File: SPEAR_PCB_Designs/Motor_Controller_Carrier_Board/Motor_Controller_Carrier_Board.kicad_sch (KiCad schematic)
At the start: 15 parts, among them J1 Conn_01x02_Pin, J2 Conn_01x02_Pin, J3 Conn_01x02_Pin, J4 JST_S4B-XH-A-1, U1 AP63203WU

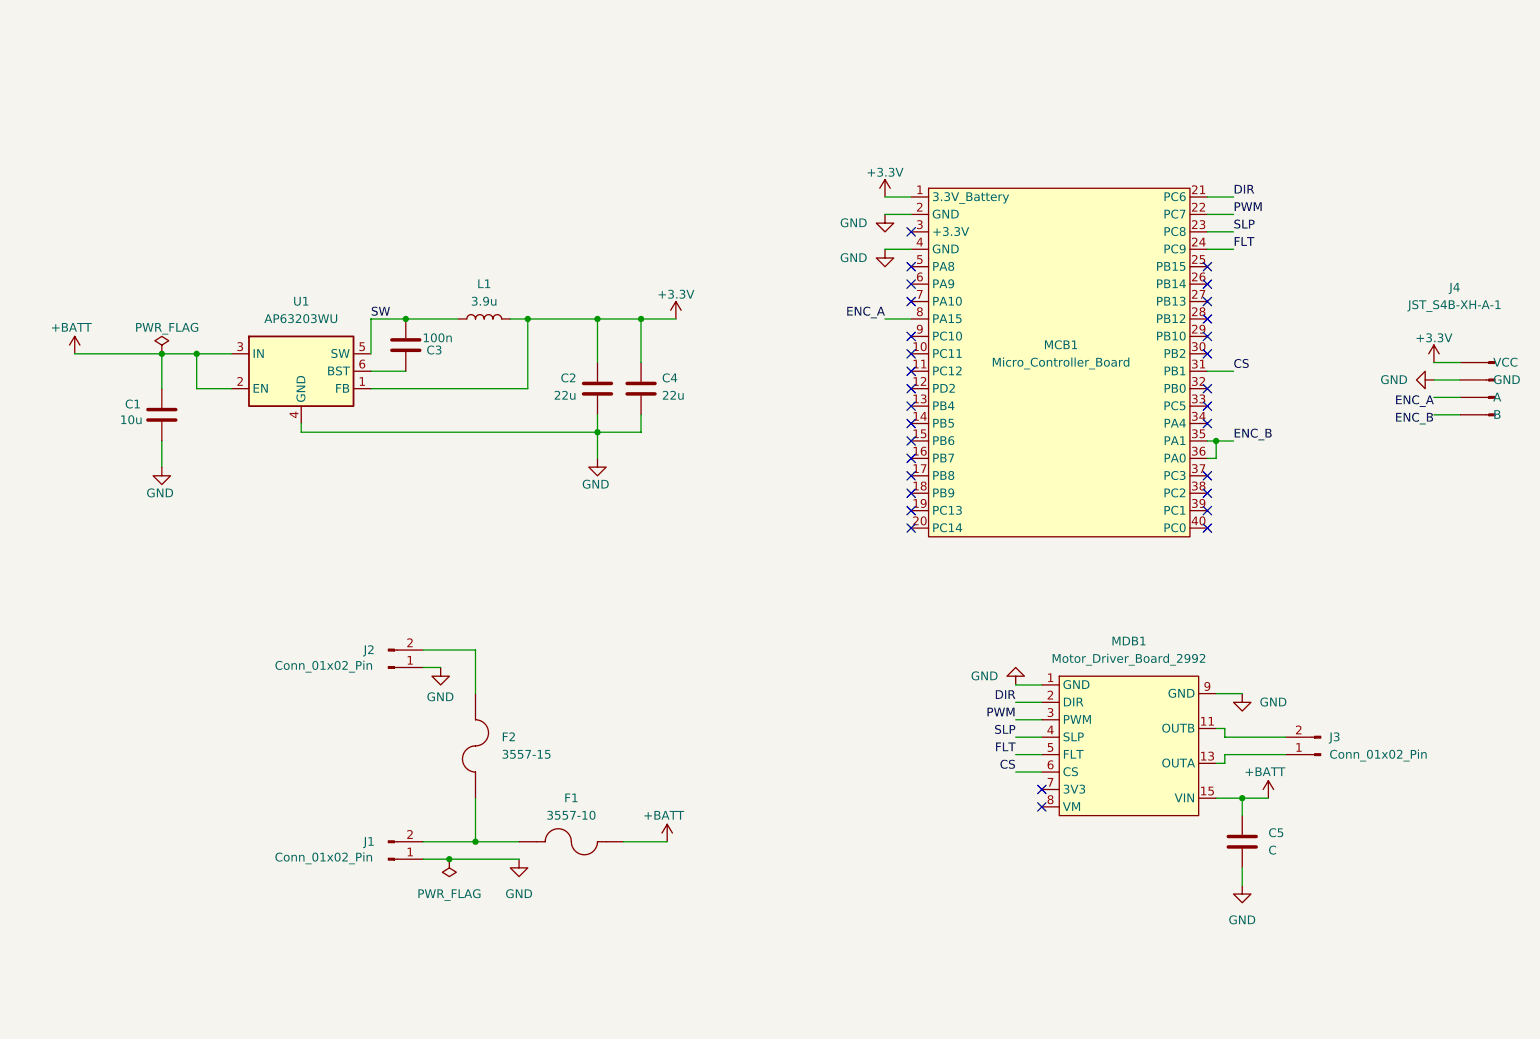
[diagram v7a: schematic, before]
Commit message: Moved power traces to the back for carrier board
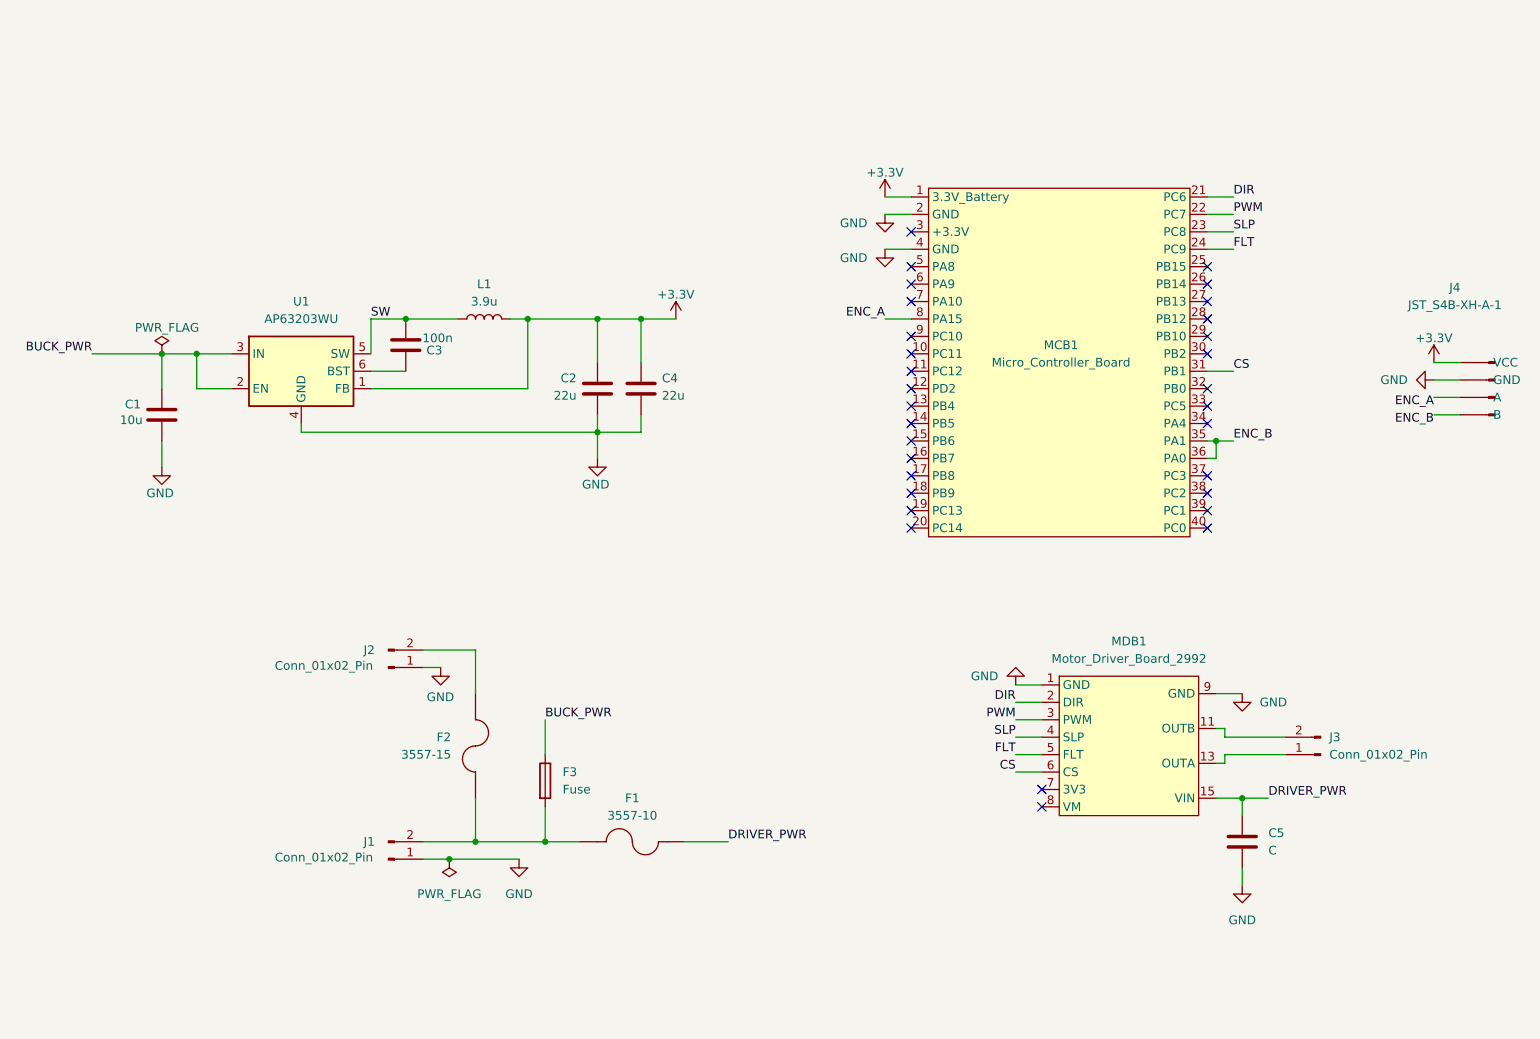
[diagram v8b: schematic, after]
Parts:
- added F3: Fuse, Motor_Controller_Carrier_Board:FUS_LITTELFUSE_392_LTF, symbol Device:Fuse
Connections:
- net at F1.1_1, F1.1_2, F2.1_1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: now also F3.2
- net +BATT renamed DRIVER_PWR
- net DRIVER_PWR: no longer C1.1, U1.2 (EN), U1.3 (IN)
- new net BUCK_PWR: C1.1, F3.1, U1.2 (EN), U1.3 (IN)
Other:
- moved on the sheet: F1
